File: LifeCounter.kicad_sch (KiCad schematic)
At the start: 0 parts

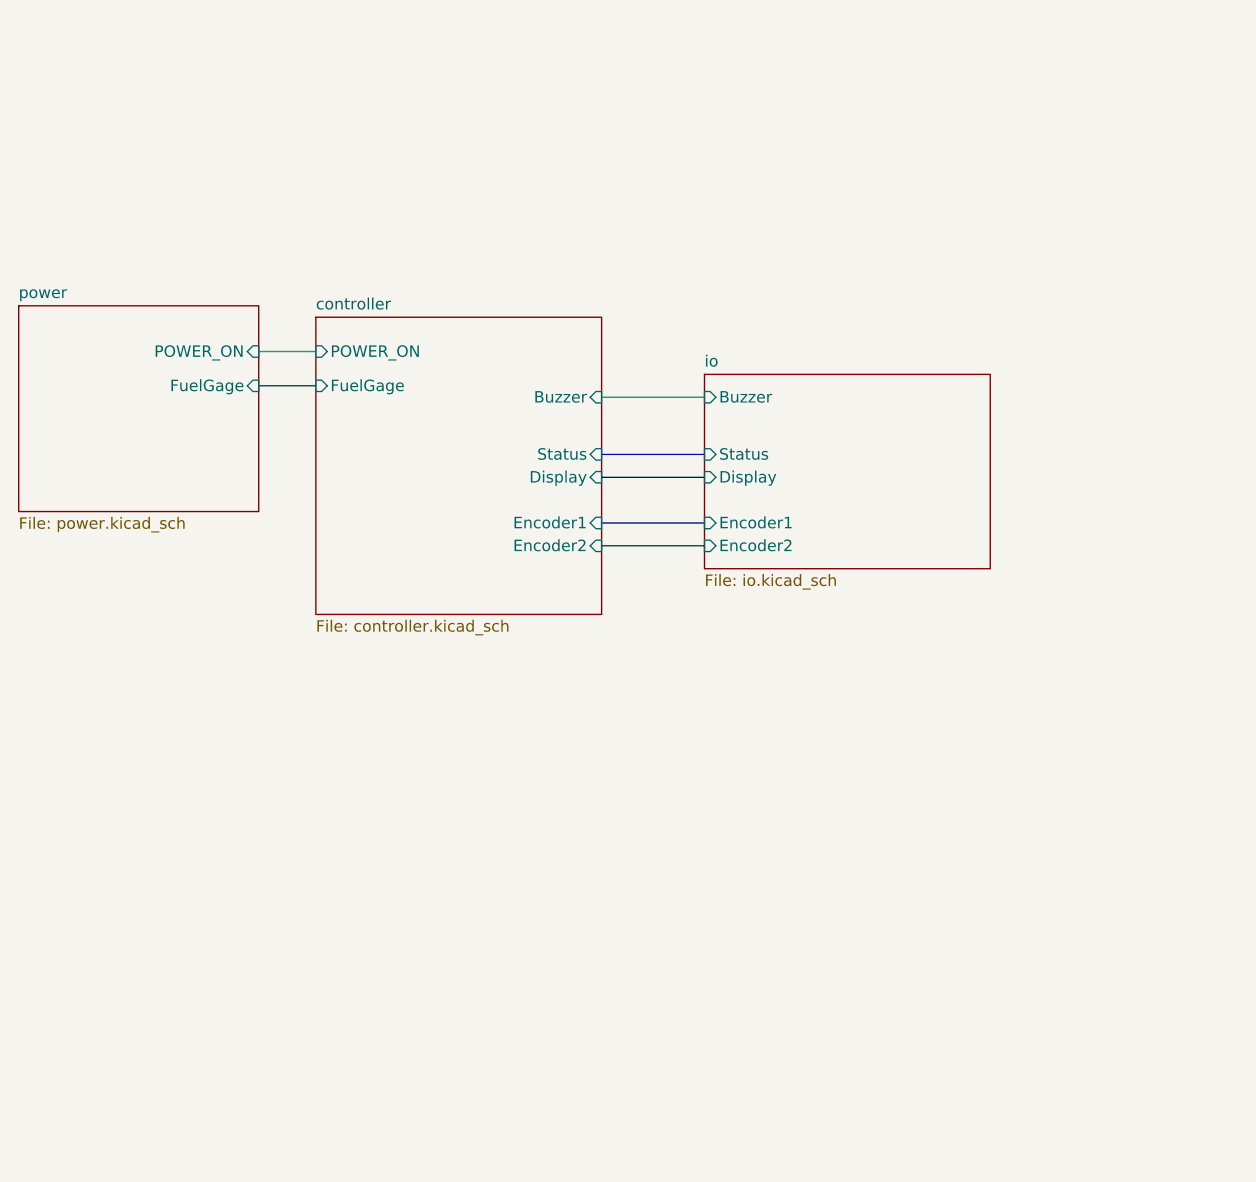
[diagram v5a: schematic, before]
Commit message: Controller wiring and schematic semantics
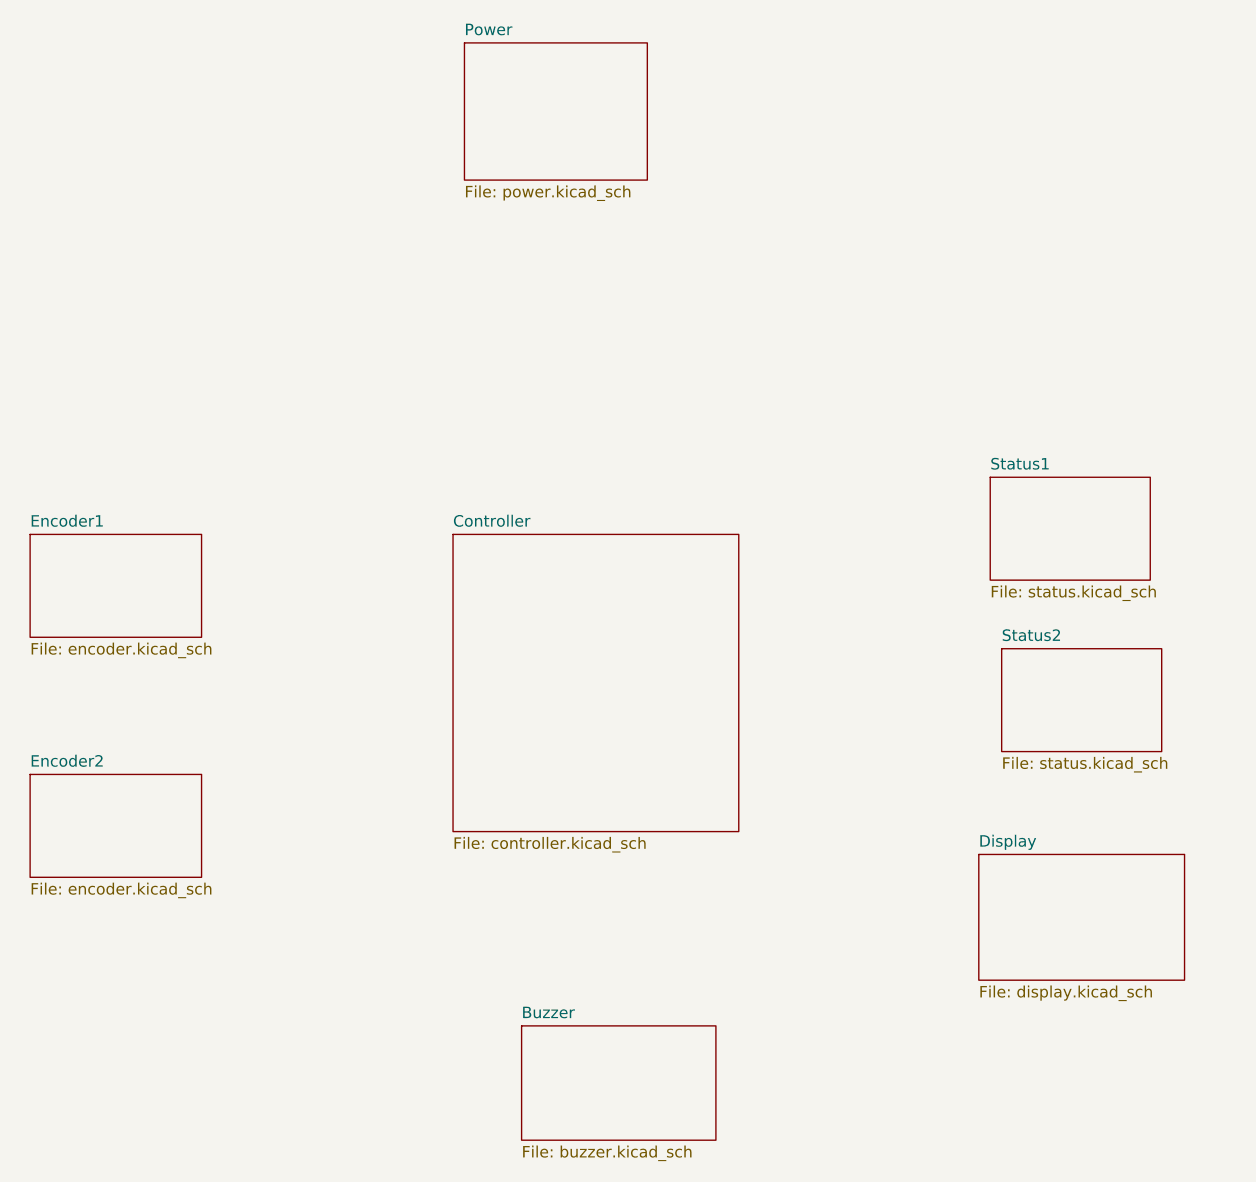
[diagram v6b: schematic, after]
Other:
- sheet controller renamed Controller
- sheet power renamed Power
- removed sheet io
- added sheet Buzzer (buzzer.kicad_sch)
- added sheet Display (display.kicad_sch)
- added sheet Encoder1 (encoder.kicad_sch)
- added sheet Encoder2 (encoder.kicad_sch)
- added sheet Status1 (status.kicad_sch)
- added sheet Status2 (status.kicad_sch)
- sheet Controller ports: added none; removed Buzzer, Display, Encoder1, Encoder2, FuelGage, POWER_ON, Status
- sheet Power ports: added none; removed FuelGage, POWER_ON

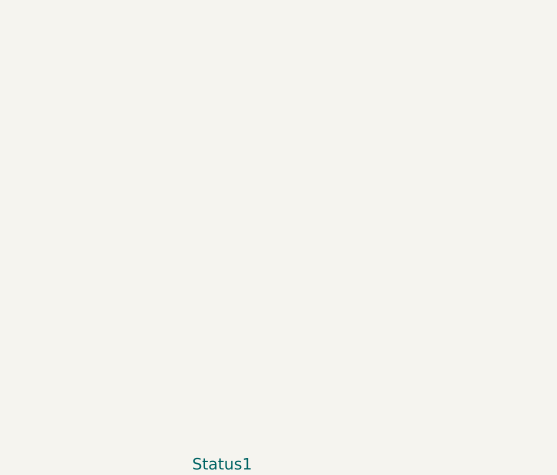
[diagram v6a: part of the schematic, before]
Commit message: Add mounting holes
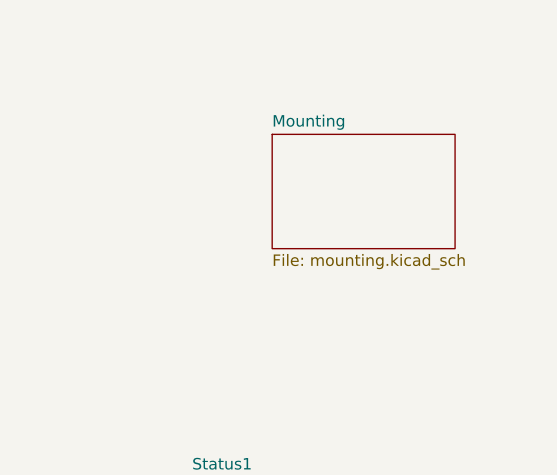
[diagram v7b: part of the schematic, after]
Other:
- added sheet Mounting (mounting.kicad_sch)
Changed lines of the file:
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@@
+	)
+	(sheet
+		(at 195.58 53.34)
+		(size 20.32 12.7)
+		(fields_autoplaced yes)
+		(stroke
+			(width 0.1524)
+			(type solid)
+		)
+		(fill
+			(color 0 0 0 0.0000)
+		)
+		(property "Sheetname" "Mounting"
+			(at 195.58 52.6284 0)
+			(effects
+				(font
+					(size 1.27 1.27)
+				)
+				(justify left bottom)
+			)
+		)
+		(property "Sheetfile" "mounting.kicad_sch"
+			(at 195.58 66.6246 0)
+			(effects
+				(font
+					(size 1.27 1.27)
+				)
+				(justify left top)
+			)
+		)
+		(instances
+			(project "LifeCounter"
+				(path "/16b3e55a-9d75-49bf-a6fe-25414eb3d7da"
+					(page "10")
+				)
+			)
+		)
 	)
 	(sheet

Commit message: Component hookup
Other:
- sheet Buzzer ports: added Buzz; removed none
- sheet Controller ports: added Encoder1{Encoder}, Encoder2{Encoder}, I2C1{I2C}, PWM, PWR_Ctrl, PWR_OK, SPI1{SPI}, Status1{Status}, Status2{Status}; removed none
- sheet Display ports: added SPI; removed none
- sheet Encoder1 ports: added Encoder; removed none
- sheet Encoder2 ports: added Encoder; removed none
- sheet Power ports: added BAT_LOW, I2C, PWR_CTRL; removed none
- sheet Status1 ports: added Status; removed none
- sheet Status2 ports: added Status; removed none
